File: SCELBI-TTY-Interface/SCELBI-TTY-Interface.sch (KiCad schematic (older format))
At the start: 12 parts, among them J1 Edge44

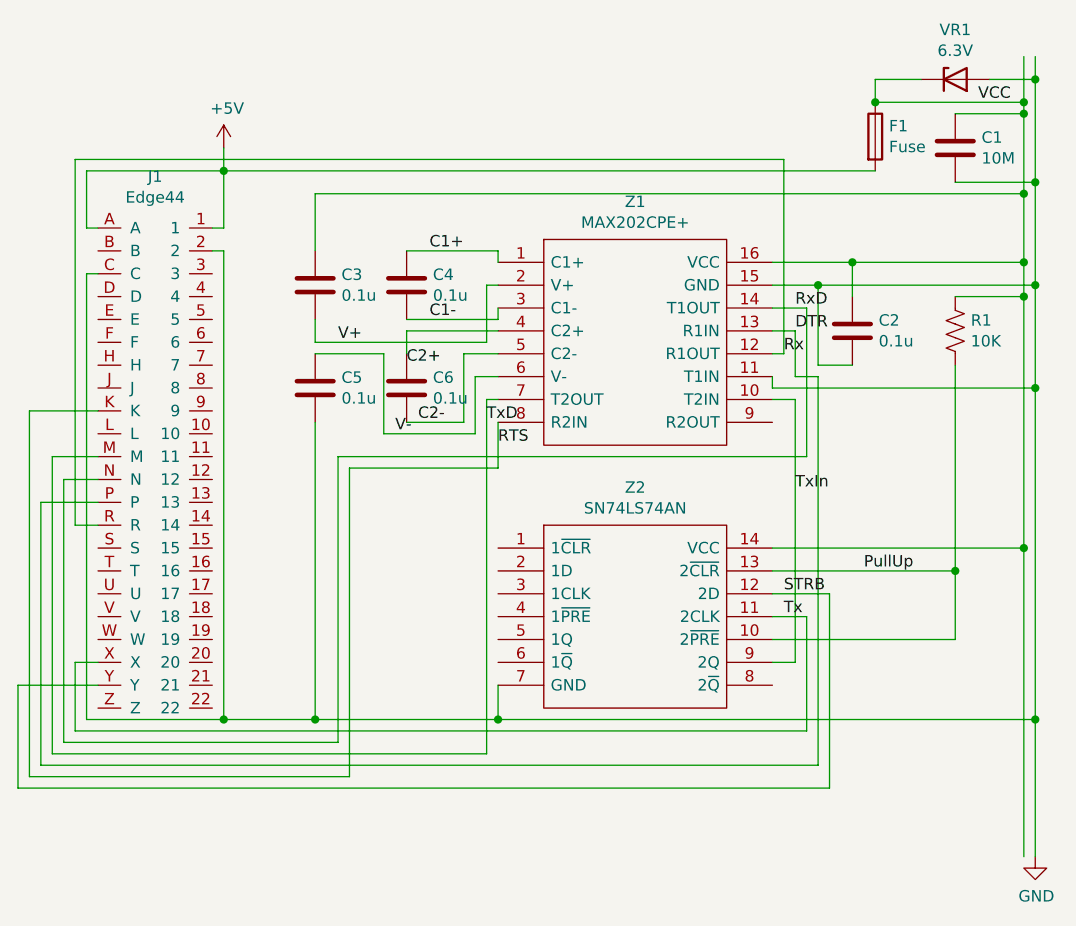
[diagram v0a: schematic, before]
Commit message: Swap strobe/tx, widen drill for supply components, relabel control signals
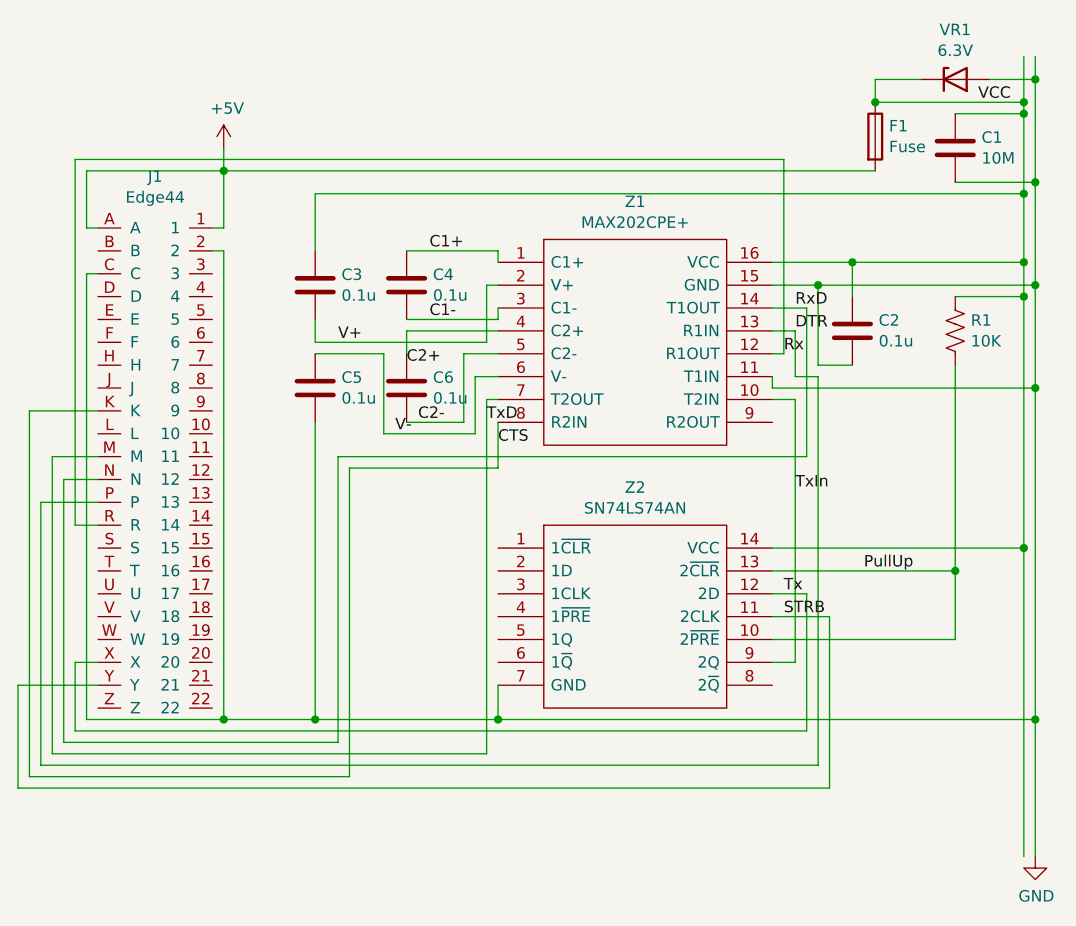
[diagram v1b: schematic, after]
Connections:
- net labels added: CTS
- net labels removed: RTS
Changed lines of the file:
@@
 $EndDescr
-$Comp
-L SamacSys_Parts:SN74LS74AN Z2
-U 1 1 606F241D
-P 5700 3150
-F 0 "Z2" H 6300 3415 50  0000 C CNN
-F 1 "SN74LS74AN" H 6300 3324 50  0000 C CNN
-F 2 "Package_DIP:DIP-14_W7.62mm_LongPads" H 6750 3250 50  0001 L CNN
-F 3 "http://www.ti.com/lit/gpn/sn74ls74a" H 6750 3150 50  0001 L CNN
-F 4 "Dual D-type pos.-edge-triggered flip-flops with preset and clear" H 6750 3050 50  0001 L CNN "Description"
-F 5 "5.08" H 6750 2950 50  0001 L CNN "Height"
-F 6 "Texas Instruments" H 6750 2850 50  0001 L CNN "Manufacturer_Name"
-F 7 "SN74LS74AN" H 6750 2750 50  0001 L CNN "Manufacturer_Part_Number"
-F 8 "595-SN74LS74AN" H 6750 2650 50  0001 L CNN "Mouser Part Number"
-F 9 "https://www.mouser.co.uk/ProductDetail/Texas-Instruments/SN74LS74AN/?qs=b0gIXGU74fP41yYZQO4%252BKQ%3D%3D" H 6750 2550 50  0001 L CNN "Mouser Price/Stock"
-F 10 "SN74LS74AN" H 6750 2450 50  0001 L CNN "Arrow Part Number"
-F 11 "https://www.arrow.com/en/products/sn74ls74an/texas-instruments" H 6750 2350 50  0001 L CNN "Arrow Price/Stock"
-	1    5700 3150
-	1    0    0    -1
-$EndComp
 $Comp
 L SamacSys_Parts:MAX202CPE+ Z1
@@
 	7000 3650 6900 3650
 Wire Wire Line
-	7000 2500 7000 3650
-Wire Wire Line
 	7050 3950 3850 3950
-Wire Wire Line
-	7050 3450 7050 3950
-Wire Wire Line
-	6900 3450 7050 3450
 Wire Wire Line
 	5700 2600 5700 2800
@@
 Wire Wire Line
 	8050 2450 8050 3900
-Wire Wire Line
-	6900 3350 7150 3350
-Wire Wire Line
-	7150 3350 7150 4200
 Wire Wire Line
 	7150 4200 3600 4200
@@
 TxD
 Text Label 5700 2700 0    50   ~ 0
-RTS
+CTS
 Text Label 7000 2900 0    50   ~ 0
 TxIn
@@
 Text Label 7300 3250 0    50   ~ 0
 PullUp
+Text Label 6950 3350 0    50   ~ 0
+Tx
 Text Label 6950 3450 0    50   ~ 0
-Tx
-Text Label 6950 3350 0    50   ~ 0
 STRB
+Wire Wire Line
+	7000 2500 7000 3650
+$Comp
+L SamacSys_Parts:SN74LS74AN Z2
+U 1 1 606F241D
+P 5700 3150
+F 0 "Z2" H 6300 3415 50  0000 C CNN
+F 1 "SN74LS74AN" H 6300 3324 50  0000 C CNN
+F 2 "Package_DIP:DIP-14_W7.62mm_LongPads" H 6750 3250 50  0001 L CNN
+F 3 "http://www.ti.com/lit/gpn/sn74ls74a" H 6750 3150 50  0001 L CNN
+F 4 "Dual D-type pos.-edge-triggered flip-flops with preset and clear" H 6750 3050 50  0001 L CNN "Description"
+F 5 "5.08" H 6750 2950 50  0001 L CNN "Height"
+F 6 "Texas Instruments" H 6750 2850 50  0001 L CNN "Manufacturer_Name"
+F 7 "SN74LS74AN" H 6750 2750 50  0001 L CNN "Manufacturer_Part_Number"
+F 8 "595-SN74LS74AN" H 6750 2650 50  0001 L CNN "Mouser Part Number"
+F 9 "https://www.mouser.co.uk/ProductDetail/Texas-Instruments/SN74LS74AN/?qs=b0gIXGU74fP41yYZQO4%252BKQ%3D%3D" H 6750 2550 50  0001 L CNN "Mouser Price/Stock"
+F 10 "SN74LS74AN" H 6750 2450 50  0001 L CNN "Arrow Part Number"
+F 11 "https://www.arrow.com/en/products/sn74ls74an/texas-instruments" H 6750 2350 50  0001 L CNN "Arrow Price/Stock"
+	1    5700 3150
+	1    0    0    -1
+$EndComp
+Wire Wire Line
+	7050 3350 6900 3350
+Wire Wire Line
+	7050 3350 7050 3950
+Wire Wire Line
+	6900 3450 7150 3450
+Wire Wire Line
+	7150 3450 7150 4200
 $EndSCHEMATC
